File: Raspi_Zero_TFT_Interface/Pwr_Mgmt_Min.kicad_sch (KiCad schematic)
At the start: 12 parts, among them Q1 SI2347DS-TI-GE3CT, Q2 SSM3J358R, U11 MCP73831-2-OT, U3 LTC4412xS6

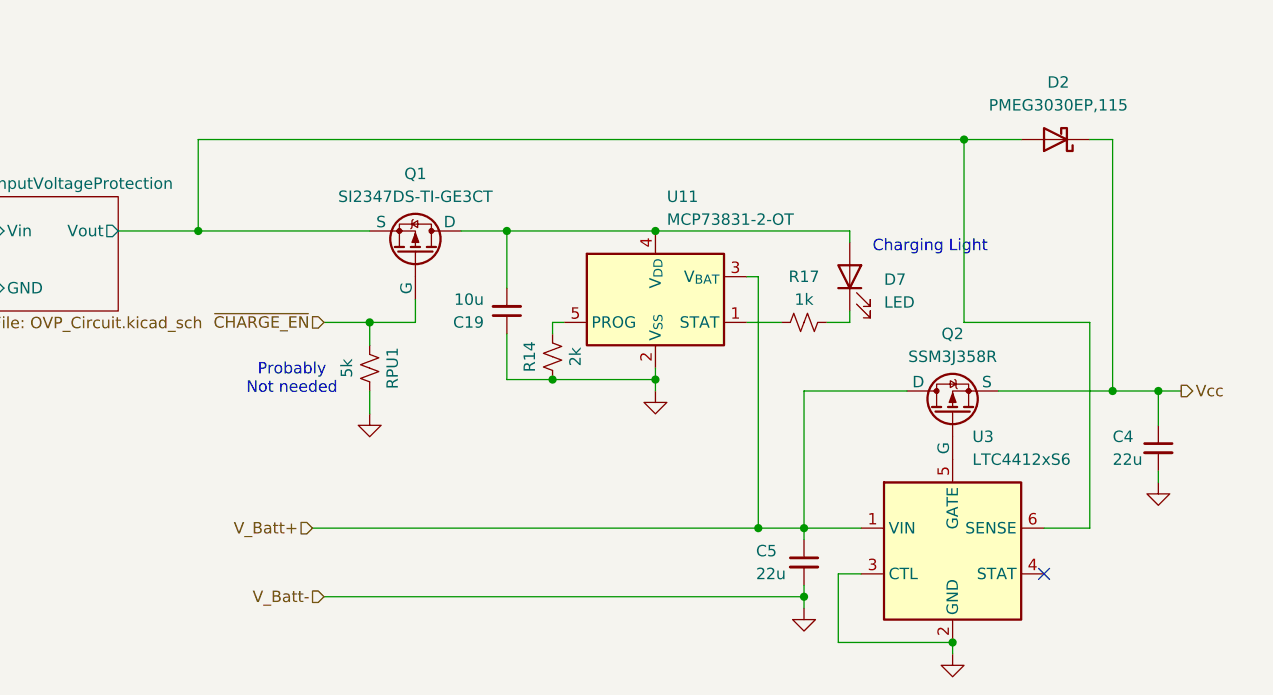
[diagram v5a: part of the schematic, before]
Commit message: Finished Rasp Board PCB Routing
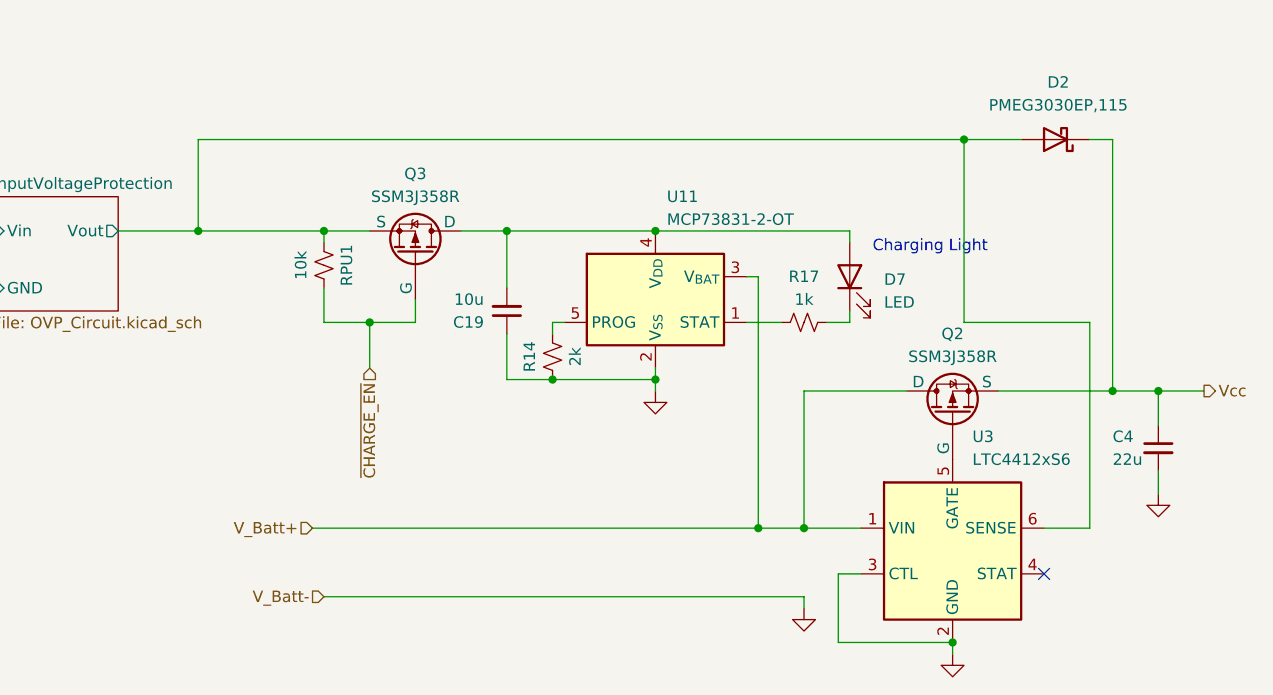
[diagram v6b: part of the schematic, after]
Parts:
- removed C5: 22u, Capacitor_SMD:C_0603_1608Metric_Pad1.08x0.95mm_HandSolder, symbol Device:C_Small
- removed Q1: SI2347DS-TI-GE3CT, Package_TO_SOT_SMD:SOT-23-3, symbol FrontEndPrototype_Rev1-rescue:SSM3J358R
- added Q3: SSM3J358R, Package_TO_SOT_SMD:SOT-23-3, symbol FrontEndPrototype_Rev1-rescue:SSM3J358R
- RPU1: value 5k -> 10k
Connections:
- net GND: no longer RPU1.2
- net InputVoltageProtection/Vout: now also RPU1.1, Q3.2 (S)
- net ~{CHARGE_EN}: now also RPU1.2, Q3.1 (G); no longer RPU1.1
- net at C19.2, D7.2 (A), U11.4 (V_{DD}): now also Q3.3 (D)
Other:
- note removed: "Probably Not needed"
- moved on the sheet: RPU1

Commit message: Final Rev3 Commit Post Submission
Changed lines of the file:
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@@
 	(text "Charging Light"
 		(exclude_from_sim no)
-		(at 130.81 45.72 0)
+		(at 125.476 41.402 0)
 		(effects
 			(font
